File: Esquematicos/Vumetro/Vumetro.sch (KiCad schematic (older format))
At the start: 13 parts

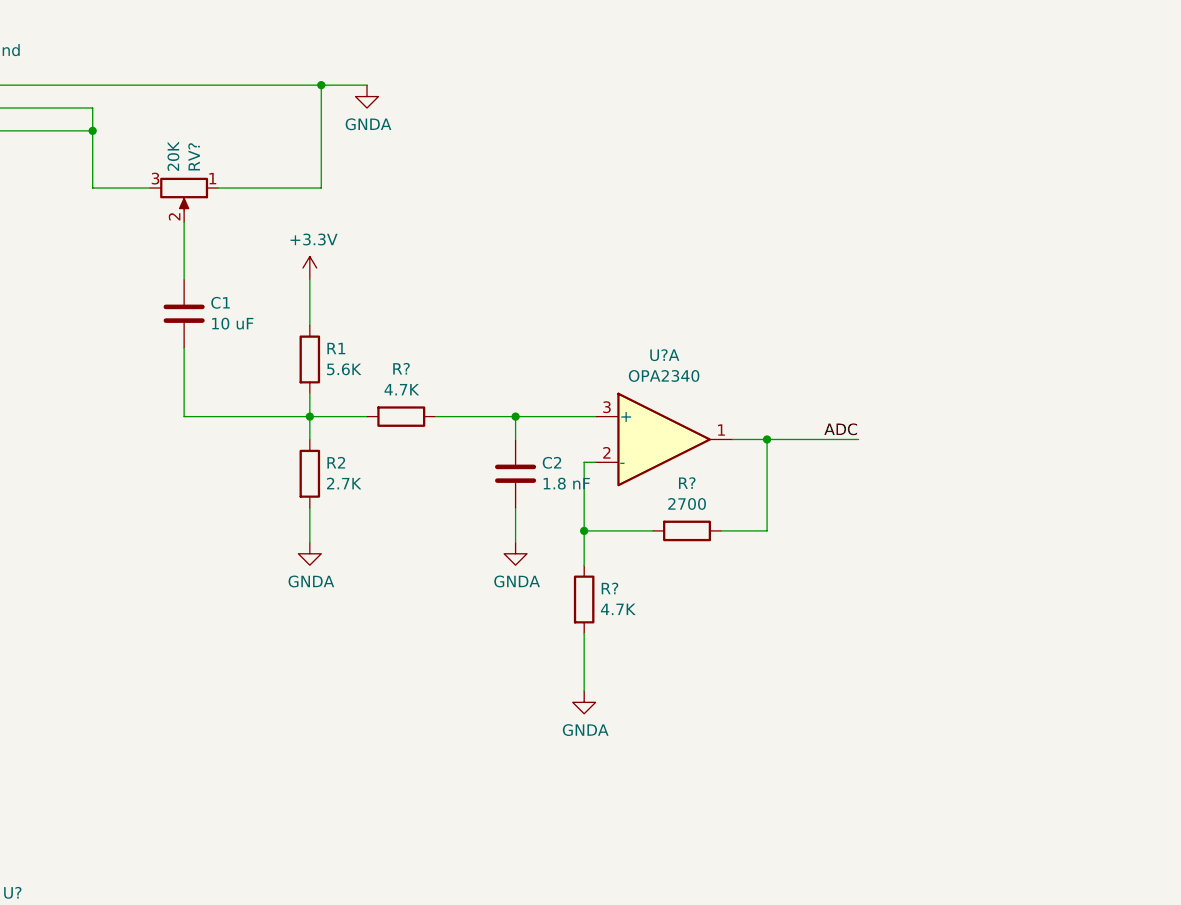
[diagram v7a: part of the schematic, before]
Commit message: modificacion esquematico
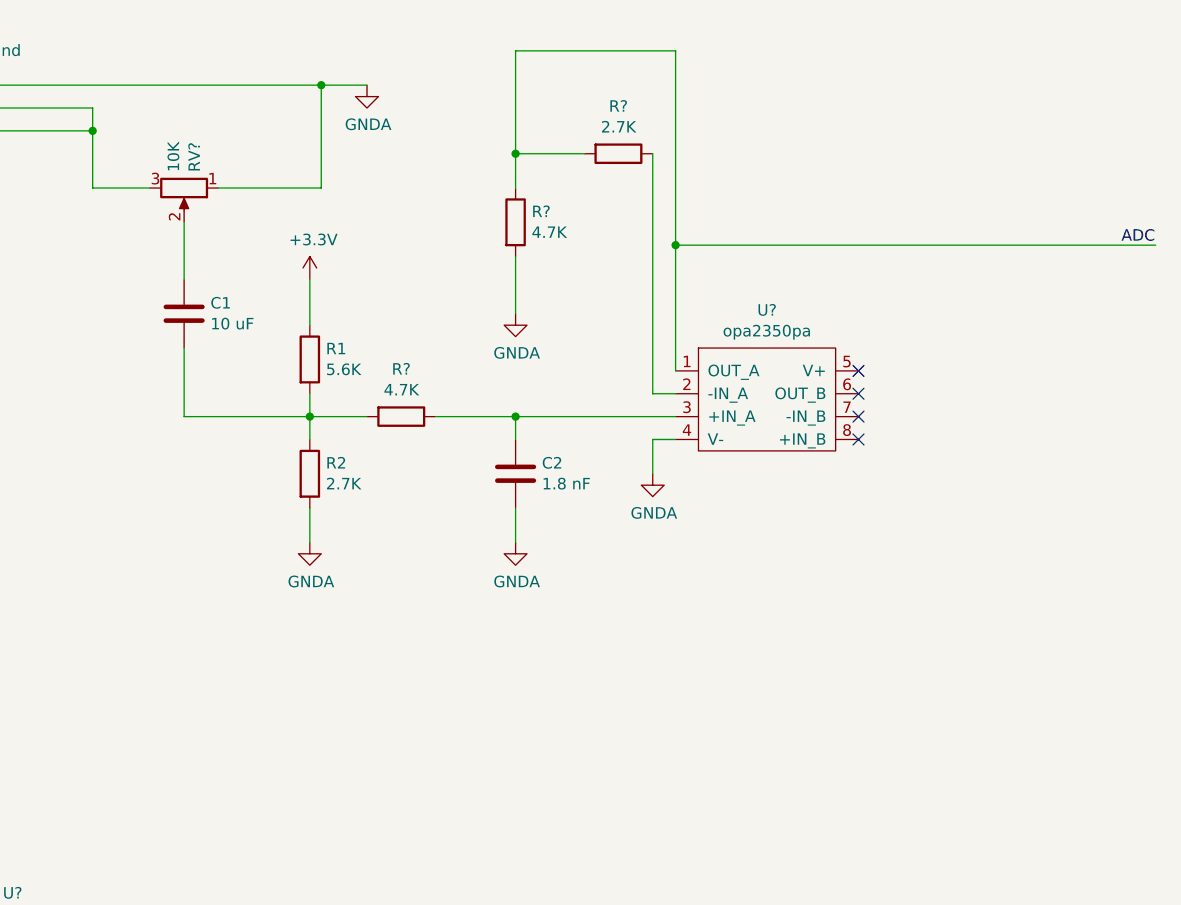
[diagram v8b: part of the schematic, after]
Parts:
- removed U?: OPA2340, symbol Amplifier_Operational:OPA2340
- added U?: opa2350pa, symbol vumetro:opa2350pa
- R?: value 2700 -> 2.7K
- RV?: value 20K -> 10K
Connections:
- wire segments 30 -> 33
- no-connect marks 0 -> 4
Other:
- moved on the sheet: R?
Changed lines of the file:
@@
 P 2850 2150
 F 0 "RV?" H 2780 2196 50  0000 R CNN
-F 1 "20K" H 2780 2105 50  0000 R CNN
+F 1 "10K" H 2780 2105 50  0000 R CNN
 F 2 "" H 2850 2150 50  0001 C CNN
 F 3 "~" H 2850 2150 50  0001 C CNN
@@
 Wire Wire Line
 	3400 3550 3400 3700
-$Comp
-L Amplifier_Operational:OPA2340 U?
-U 1 1 5BD1E25D
-P 4950 3250
-F 0 "U?" H 4950 3617 50  0000 C CNN
-F 1 "OPA2340" H 4950 3526 50  0000 C CNN
-F 2 "" H 4950 3250 50  0001 C CNN
-F 3 "http://www.ti.com/lit/ds/symlink/opa4340.pdf" H 4950 3250 50  0001 C CNN
-	1    4950 3250
-	1    0    0    -1
-$EndComp
 Wire Wire Line
 	3400 3150 3650 3150
-Wire Wire Line
-	4300 3150 4650 3150
 Connection ~ 4300 3150
 $Comp
 L Device:R R?
 U 1 1 5BD1FFCF
-P 4600 3950
-F 0 "R?" H 4670 3996 50  0000 L CNN
-F 1 "4.7K" H 4670 3905 50  0000 L CNN
-F 2 "" V 4530 3950 50  0001 C CNN
-F 3 "~" H 4600 3950 50  0001 C CNN
-	1    4600 3950
-	1    0    0    -1
-$EndComp
-Wire Wire Line
-	4650 3350 4600 3350
+P 4300 2300
+F 0 "R?" H 4370 2346 50  0000 L CNN
+F 1 "4.7K" H 4370 2255 50  0000 L CNN
+F 2 "" V 4230 2300 50  0001 C CNN
+F 3 "~" H 4300 2300 50  0001 C CNN
+	1    4300 2300
+	1    0    0    -1
+$EndComp
 $Comp
 L Device:R R?
 U 1 1 5BD204D6
-P 5050 3650
-F 0 "R?" V 4843 3650 50  0000 C CNN
-F 1 "2700" V 4934 3650 50  0000 C CNN
-F 2 "" V 4980 3650 50  0001 C CNN
-F 3 "~" H 5050 3650 50  0001 C CNN
-	1    5050 3650
+P 4750 2000
+F 0 "R?" V 4543 2000 50  0000 C CNN
+F 1 "2.7K" V 4634 2000 50  0000 C CNN
+F 2 "" V 4680 2000 50  0001 C CNN
+F 3 "~" H 4750 2000 50  0001 C CNN
+	1    4750 2000
 	0    1    1    0
 $EndComp
 Wire Wire Line
-	4600 3350 4600 3650
-Wire Wire Line
-	4900 3650 4600 3650
-Connection ~ 4600 3650
-Wire Wire Line
-	4600 3650 4600 3800
-Wire Wire Line
-	5200 3650 5400 3650
-Wire Wire Line
-	5400 3650 5400 3250
-Wire Wire Line
-	5400 3250 5250 3250
+	4600 2000 4300 2000
+Connection ~ 4300 2000
+Wire Wire Line
+	4300 2000 4300 2150
 $Comp
 L power:GNDA #PWR0105
 U 1 1 5BD20C9D
-P 4600 4350
-F 0 "#PWR0105" H 4600 4100 50  0001 C CNN
-F 1 "GNDA" H 4605 4177 50  0000 C CNN
-F 2 "" H 4600 4350 50  0001 C CNN
-F 3 "" H 4600 4350 50  0001 C CNN
-	1    4600 4350
-	1    0    0    -1
-$EndComp
-Wire Wire Line
-	4600 4100 4600 4350
+P 4300 2700
+F 0 "#PWR0105" H 4300 2450 50  0001 C CNN
+F 1 "GNDA" H 4305 2527 50  0000 C CNN
+F 2 "" H 4300 2700 50  0001 C CNN
+F 3 "" H 4300 2700 50  0001 C CNN
+	1    4300 2700
+	1    0    0    -1
+$EndComp
+Wire Wire Line
+	4300 2450 4300 2700
 $Comp
 L Device:C C1
@@
 Wire Wire Line
 	2850 2850 2850 3150
-Wire Wire Line
-	5400 3250 5800 3250
-Connection ~ 5400 3250
-Text Label 5650 3250 0    50   ~ 0
+Text Label 6950 2400 0    50   ~ 0
 ADC
 $Comp
@@
 	-1   0    0    -1
 $EndComp
+$Comp
+L vumetro:opa2350pa U?
+U 1 1 5BD9369A
+P 5400 2750
+F 0 "U?" H 5400 2815 50  0000 C CNN
+F 1 "opa2350pa" H 5400 2724 50  0000 C CNN
+F 2 "" H 5400 2800 50  0001 C CNN
+F 3 "" H 5400 2800 50  0001 C CNN
+	1    5400 2750
+	1    0    0    -1
+$EndComp
+Wire Wire Line
+	4300 3150 5000 3150
+Wire Wire Line
+	4900 2000 4900 3050
+Wire Wire Line
+	4900 3050 5000 3050
+Wire Wire Line
+	5000 2950 5000 2400
+Wire Wire Line
+	5000 2400 7100 2400
+Wire Wire Line
+	4300 1550 5000 1550
+Wire Wire Line
+	5000 1550 5000 2400
+Wire Wire Line
+	4300 1550 4300 2000
+Connection ~ 5000 2400
+$Comp
+L power:GNDA #PWR?
+U 1 1 5BD9D42A
+P 4900 3400
+F 0 "#PWR?" H 4900 3150 50  0001 C CNN
+F 1 "GNDA" H 4905 3227 50  0000 C CNN
+F 2 "" H 4900 3400 50  0001 C CNN
+F 3 "" H 4900 3400 50  0001 C CNN
+	1    4900 3400
+	1    0    0    -1
+$EndComp
+Wire Wire Line
+	4900 3400 4900 3250
+Wire Wire Line
+	4900 3250 5000 3250
+NoConn ~ 5800 2950
+NoConn ~ 5800 3050
+NoConn ~ 5800 3150
+NoConn ~ 5800 3250
 $EndSCHEMATC
